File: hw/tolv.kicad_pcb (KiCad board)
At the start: 2 copper layers, 69.3 x 80 mm, 104 parts, among them J4 DEBUG, Q1 AO3400A, Q10 AO3400A, Q11 AO3400A, Q12 AO3400A, Q13 AO3400A, Q14 AO3400A, Q15 AO3400A, Q16 AO3400A, Q17 AO3400A, Q18 AO3400A, Q19 AO3400A, Q2 AO3400A, Q20 AO3400A, Q21 AO3400A, Q22 AO3400A, Q23 AO3400A, Q24 AO3400A, Q25 AO3400A, Q26 AO3400A, Q27 AO3400A, Q28 AO3400A, Q29 AO3400A, Q3 AO3400A, Q30 AO3400A, Q31 AO3400A, Q32 AO3400A, Q33 AO3400A, Q34 AO3400A, Q35 AO3400A, Q36 AO3400A, Q37 AO3400A, Q38 AO3400A, Q39 AO3400A, Q4 AO3400A, Q40 AO3400A, Q41 AO3400A, Q42 AO3400A, Q43 AO3400A, Q44 AO3400A, Q45 AO3400A, Q46 AO3400A, Q47 AO3400A, Q48 AO3400A, Q5 AO3400A, Q6 AO3400A, Q7 AO3400A, Q8 AO3400A, Q9 AO3400A, U1 74HC595, U13 MAX3485, U14 STM32F030F4Px, U2 74HC595, U3 74HC595, U4 74HC595, U5 74HC595, U6 74HC595, U7 AMS1117-3.3, U9 INA180A2, Y1 8 MHz

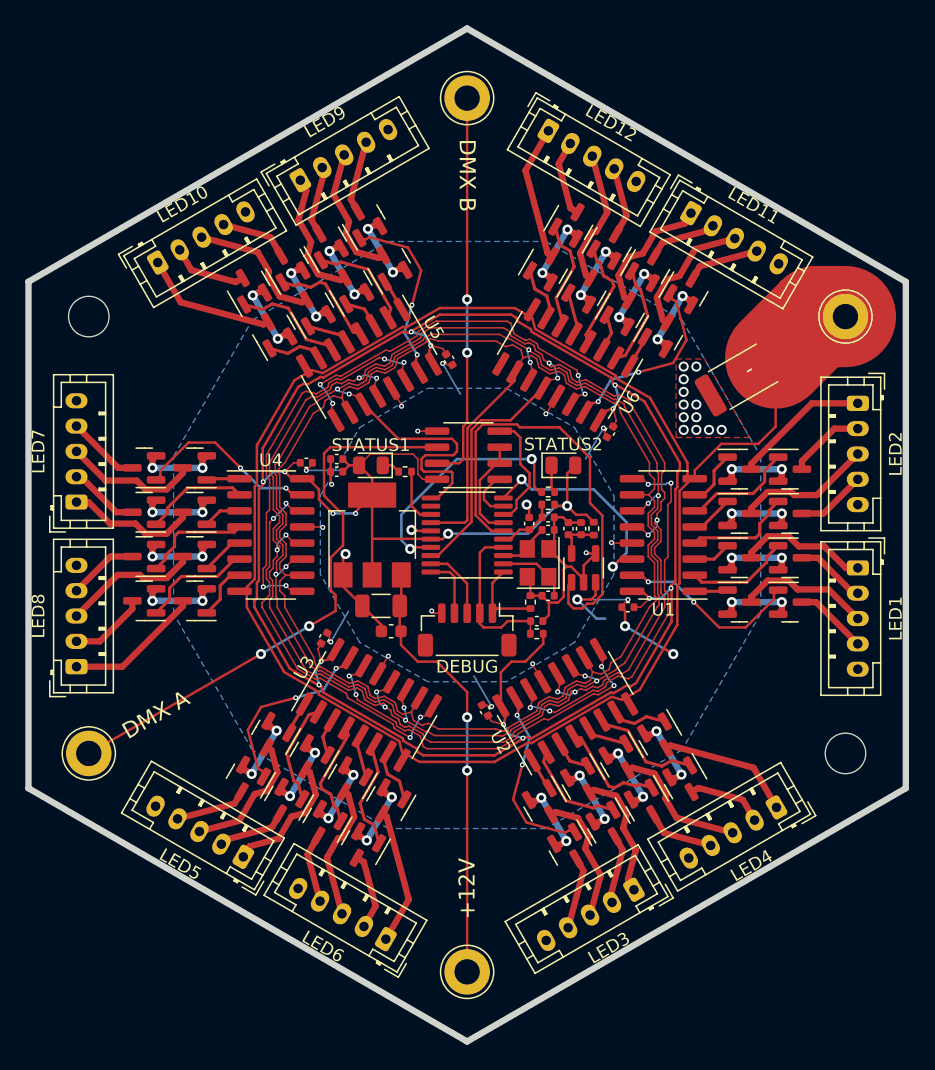
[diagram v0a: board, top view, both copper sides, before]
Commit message: Switch to switching regulator
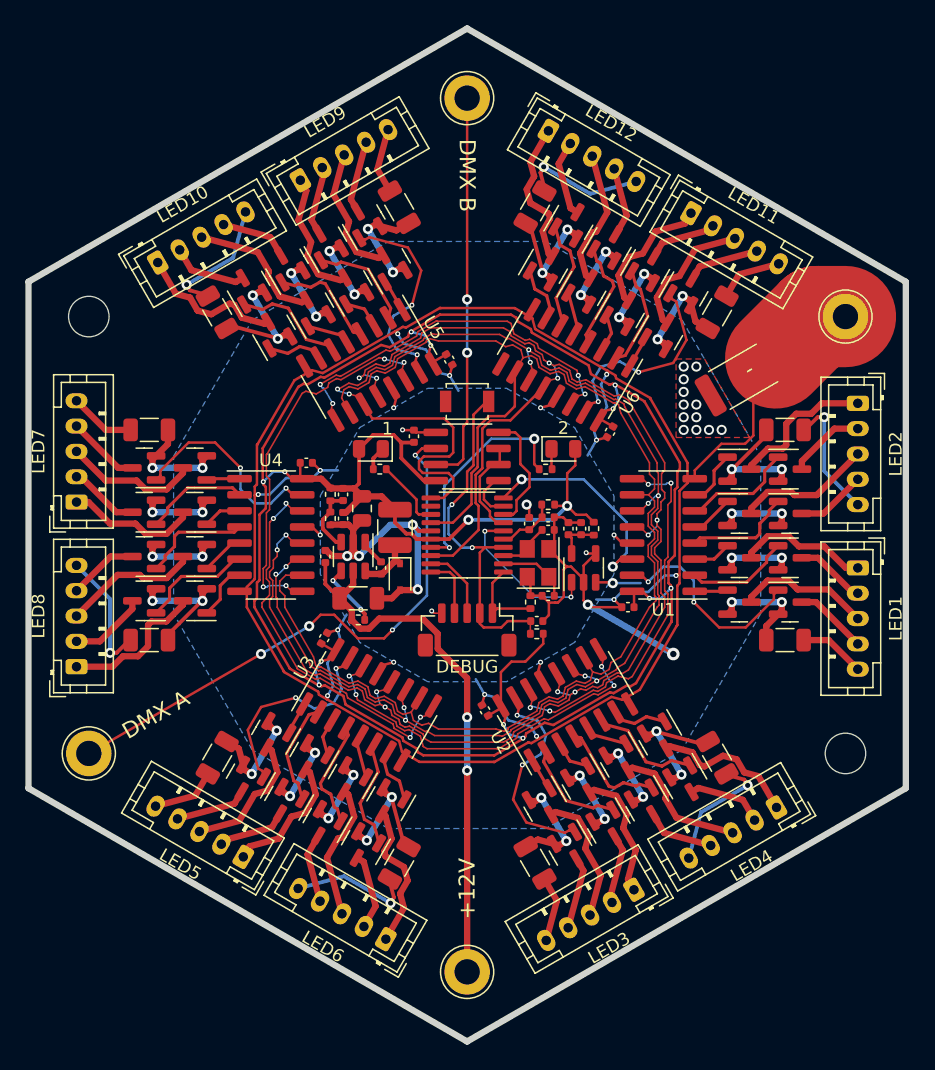
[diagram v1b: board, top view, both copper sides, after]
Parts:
- removed STATUS1, STATUS2: LED, LED_SMD:LED_0805_2012Metric
- added 1: LED, LED_SMD:LED_0805_2012Metric, F.Cu at (-7.60, -6.80)
- added 2: LED, LED_SMD:LED_0805_2012Metric, F.Cu at (7.60, -6.80)
- added C15: 22u 25V, Capacitor_SMD:C_0805_2012Metric, F.Cu at (-8.30, -2.10)
- added C17: 100n, Capacitor_SMD:C_0402_1005Metric, F.Cu at (-9.80, -1.30)
- added C21: 10u 50V, Capacitor_SMD:C_1206_3216Metric, F.Cu at (25.1, 8.30)
- added C22: 10u 50V, Capacitor_SMD:C_1206_3216Metric, F.Cu at (25.1, -8.30)
- added C23: 10u 50V, Capacitor_SMD:C_1206_3216Metric, F.Cu at (5.36, 25.9)
- added C24: 10u 50V, Capacitor_SMD:C_1206_3216Metric, F.Cu at (19.7, 17.6)
- added C25: 10u 50V, Capacitor_SMD:C_1206_3216Metric, F.Cu at (-19.7, 17.6)
- added C26: 10u 50V, Capacitor_SMD:C_1206_3216Metric, F.Cu at (-5.36, 25.9)
- added C27: 10u 50V, Capacitor_SMD:C_1206_3216Metric, F.Cu at (-25.1, -8.30)
- added C28: 10u 50V, Capacitor_SMD:C_1206_3216Metric, F.Cu at (-25.1, 8.30)
- added C29: 10u 50V, Capacitor_SMD:C_1206_3216Metric, F.Cu at (-5.36, -25.9)
- added C30: 10u 50V, Capacitor_SMD:C_1206_3216Metric, F.Cu at (-19.7, -17.6)
- added C31: 10u 50V, Capacitor_SMD:C_1206_3216Metric, F.Cu at (19.7, -17.6)
- added C32: 10u 50V, Capacitor_SMD:C_1206_3216Metric, F.Cu at (5.36, -25.9)
- added C33: 100n, Capacitor_SMD:C_0402_1005Metric, F.Cu at (-4.20, -7.80)
- added D1: 1N5819WS, Diode_SMD:D_SOD-323, F.Cu at (-5.30, 3.30)
- added L1: 47uH 390mA, Inductor_SMD:L_1210_3225Metric, F.Cu at (-5.70, -0.60)
- added R5: 47k, Resistor_SMD:R_0402_1005Metric, F.Cu at (-8.60, 6.70)
- added R6: 100k, Resistor_SMD:R_0402_1005Metric, F.Cu at (-10.8, -3.21)
- added R7: 22k, Resistor_SMD:R_0402_1005Metric, F.Cu at (-10.8, -1.30)
- added SW1: SW_Push, Button_Switch_SMD:SW_SPST_B3U-1000P, F.Cu at (0.00, -10.6)
- C10: value 100n -> 22p
- C7: value 10u -> 10u 50V
- C8: value 1u -> 100n 50V; footprint Capacitor_SMD:C_0603_1608Metric -> Capacitor_SMD:C_0402_1005Metric
- C9: value 1u -> 100n 50V
- U7: value AMS1117-3.3 -> SY8291; footprint Package_TO_SOT_SMD:SOT-223-3_TabPin2 -> Package_TO_SOT_SMD:TSOT-23-6
- moved C9 8.37 mm to (-6.80, 2.60), turned to 90 degrees
- moved C8 7.86 mm to (-11.2, 1.70), turned to 90 degrees
- moved C10 2.84 mm to (-9.80, -3.20), turned to -90 degrees
- moved U7 2.27 mm to (-9.00, 1.70), turned to -90 degrees
- moved R14 2.01 mm to (-6.90, -5.20)
- moved C7 1.90 mm to (-8.60, 5.00), turned to 0 degrees
- moved R4 1.81 mm to (6.20, -5.20)
- moved U13 0.14 mm to (0.00, -6.20)
- turned H1 to 150 degrees
- turned H2 to -30 degrees
- turned PAD1 to 90 degrees
- turned PAD2 to -150 degrees
- turned PAD3 to -90 degrees
- turned PAD4 to 30 degrees
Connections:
- C10 pad 2: GND -> Net-(C10-Pad2)
- C9 pad 1: +3V3 -> Net-(C9-Pad1)
- C9 pad 2: GND -> Net-(C9-Pad2)
- U7 pad 1: GND -> Net-(C9-Pad2)
- U7 pad 2: +3V3 -> GND
- U7 pad 3: +12V -> Net-(C10-Pad2)
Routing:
- net +12V: track 34.5 -> 134.6 mm, vias 2 -> 8
- net GND: track 209.0 -> 257.8 mm, vias 21 -> 28
- net GNDPWR: track 152.0 -> 190.6 mm
- net /MEASURE: track 35.9 -> 12.4 mm, vias 0 -> 2
- net /STROBE: track 147.0 -> 127.6 mm
- net /CLR: track 129.4 -> 112.0 mm
- net /SCLK: track 139.2 -> 121.8 mm
- net /RESET: track 13.0 -> 28.3 mm, vias 0 -> 2
- net Net-(C10-Pad2): track 0.00 -> 5.35 mm
- net Net-(R5-Pad1): track 0.00 -> 5.17 mm, vias 0 -> 2
- net Net-(C9-Pad1): track 0.00 -> 4.70 mm
- net +3V3: track 200.2 -> 197.3 mm, vias 16 -> 14
- net /STATUS2: track 19.8 -> 17.7 mm
- net Net-(C9-Pad2): track 0.00 -> 2.08 mm
- net Net-(Q4-Pad1): track 14.7 -> 16.7 mm
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- added copper zone on F.Cu, net GND
